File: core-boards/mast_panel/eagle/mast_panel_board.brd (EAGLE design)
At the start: 63.5 x 47.9 mm, 28 parts, among them J1 2-PIN_2MM-V, J4 4-PIN_2MM-H, U1 ATMEGA328P-AUR, U3 MCP2551T-I/SN

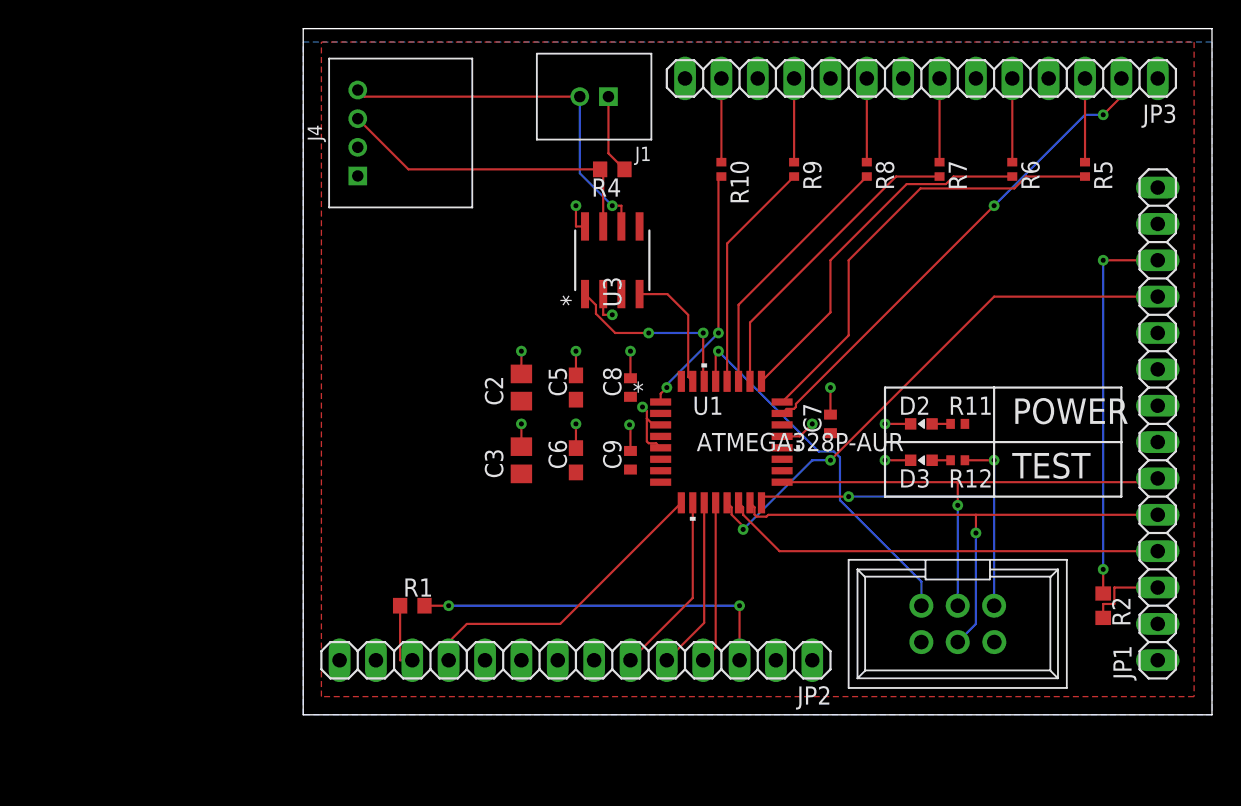
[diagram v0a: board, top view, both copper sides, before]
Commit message: 2/16/20
Cleaned up some things, added surface mount reset button
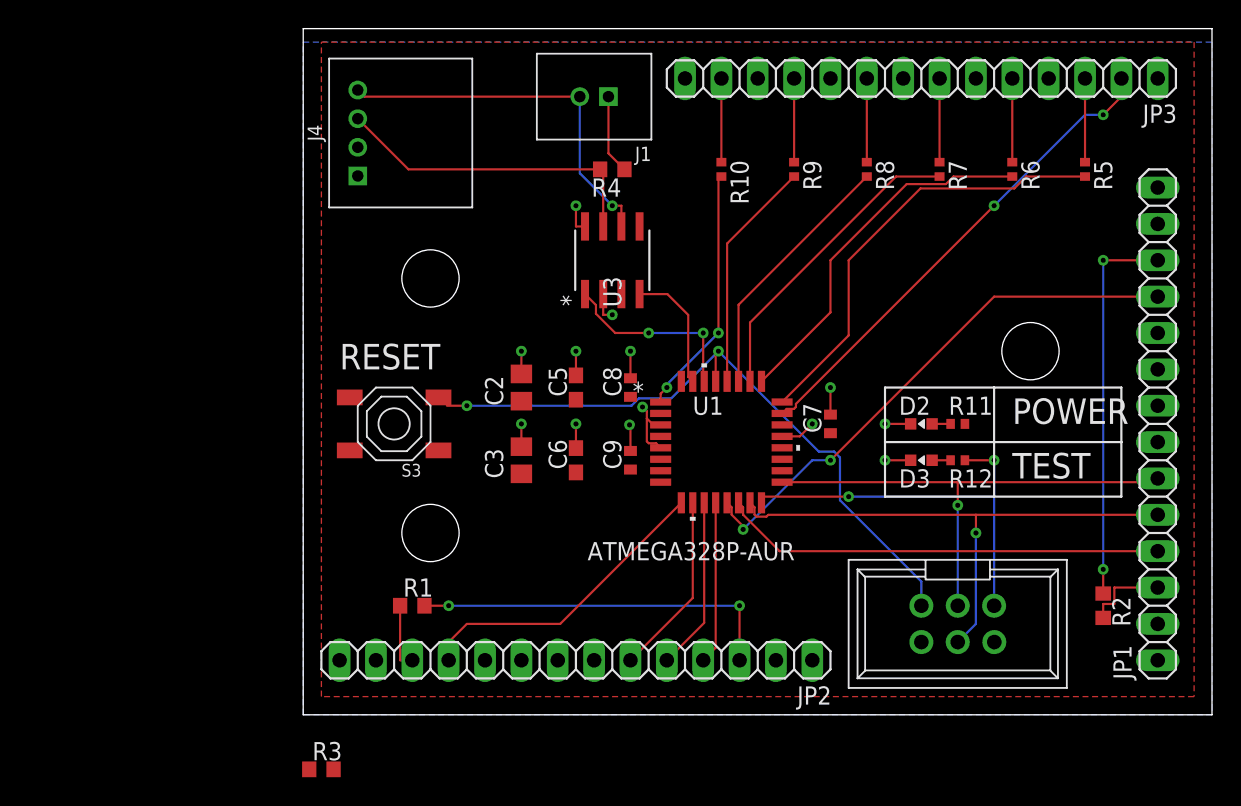
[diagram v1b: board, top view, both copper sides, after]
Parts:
- added R3: 10kO, rcl:R0603
- added S3: SKQGADE010, rgb-led:SW4-SMD-5.2X5.2X1.5MM
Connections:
- net MBED_CAN_RD/1.5C renamed MBED_CAN_RD
- net MBED_CAN_TD/1.5C renamed MBED_CAN_TD
- net +5V: now also R3.2
- net GND: now also S3.4
- net RESET: now also R3.1, S3.1
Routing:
- net RESET: track 26.6 -> 47.1 mm, vias 1 -> 2
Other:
- board text added: "RESET"
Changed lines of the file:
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@@
 <drawing>
 <settings>
-<setting alwaysvectorfont="yes"/>
+<setting alwaysvectorfont="no"/>
 <setting verticaltext="up"/>
 </settings>
-<grid distance="50" unitdist="mil" unit="mil" style="lines" multiple="1" display="no" altdistance="5" altunitdist="mil" altunit="mil"/>
+<grid distance="50" unitdist="mil" unit="mm" style="lines" multiple="1" display="no" altdistance="5" altunitdist="mil" altunit="mil"/>
 <layers>
 <layer number="1" name="Top" color="4" fill="1" visible="yes" active="yes"/>
@@
 <text x="72.39" y="25.4" size="1.778" layer="21" font="vector">POWER</text>
 <text x="72.39" y="21.59" size="1.778" layer="21" font="vector">TEST</text>
+<text x="25.4" y="29.21" size="1.778" layer="21" font="vector">RESET</text>
+<hole x="31.75" y="35.56" drill="4"/>
+<hole x="31.75" y="17.78" drill="4"/>
+<hole x="73.66" y="30.48" drill="4"/>
 </plain>
 <attributes>
@@
 <attribute name="MANUFACTURER_PART_NUMBER" value="ATMEGA328P-AUR" x="91.44" y="17.78" size="1.778" layer="27" display="off"/>
 <attribute name="NAME" x="50.0634" y="26.035" size="1.27" layer="25" font="vector" ratio="6" rot="SR0"/>
-<attribute name="VALUE" x="50.3428" y="23.495" size="1.27" layer="21" font="vector" ratio="6" rot="SR0"/>
+<attribute name="VALUE" x="42.7228" y="15.875" size="1.27" layer="21" font="vector" ratio="6" rot="SR0"/>
 <attribute name="VENDOR" value="Atmel" x="91.44" y="17.78" size="1.778" layer="27" display="off"/>
 </element>
@@
 </element>
 <element name="PROG" library="lcd-buzzer" package="2X3SHROUDED" value="ICSP Connector" x="68.58" y="11.43" smashed="yes"/>
+<element name="S3" library="rgb-led" package="SW4-SMD-5.2X5.2X1.5MM" value="SKQGADE010" x="29.21" y="25.4" smashed="yes" rot="R180">
+<attribute name="MPN" value="SKQGADE010" x="39.37" y="15.24" size="1.778" layer="27" rot="R180" display="off"/>
+<attribute name="NAME" x="31.115" y="22.606" size="0.889" layer="25" ratio="11" rot="R180"/>
+<attribute name="VALUE" x="31.115" y="29.083" size="0.889" layer="27" ratio="11" rot="R180"/>
+</element>
+<element name="R3" library="rcl" library_urn="urn:adsk.eagle:library:334" package="R0603" package3d_urn="urn:adsk.eagle:package:23555/3" value="10kO" x="24.13" y="1.27" smashed="yes">
+<attribute name="NAME" x="23.495" y="1.905" size="1.27" layer="25"/>
+<attribute name="POPULARITY" value="77" x="24.13" y="1.27" size="1.778" layer="27" display="off"/>
+<attribute name="SPICEPREFIX" value="R" x="24.13" y="1.27" size="1.778" layer="27" display="off"/>
+<attribute name="VALUE" x="23.495" y="-0.635" size="1.27" layer="27"/>
+</element>
 </elements>
 <signals>
@@
 </polygon>
 <contactref element="PROG" pad="+5V"/>
+<contactref element="R3" pad="2"/>
+<wire x1="82.55" y1="39.37" x2="82.55" y2="49.53" width="0" layer="19" extent="1-1"/>
+<wire x1="69.08" y1="25.4" x2="82.55" y2="39.37" width="0" layer="19" extent="1-1"/>
+<wire x1="59.69" y1="24.75" x2="69.08" y2="25.4" width="0" layer="19" extent="1-1"/>
+<wire x1="56.3118" y1="22.13" x2="59.69" y2="24.75" width="0" layer="19" extent="1-1"/>
+<wire x1="47.8282" y1="22.93" x2="56.3118" y2="22.13" width="0" layer="19" extent="1-1"/>
+<wire x1="47.8282" y1="24.53" x2="47.8282" y2="22.93" width="0" layer="19" extent="1-1"/>
+<wire x1="45.72" y1="22.21" x2="47.8282" y2="22.93" width="0" layer="19" extent="1-1"/>
+<wire x1="45.72" y1="27.29" x2="47.8282" y2="24.53" width="0" layer="19" extent="1-1"/>
+<wire x1="41.91" y1="27.09" x2="45.72" y2="27.29" width="0" layer="19" extent="1-1"/>
+<wire x1="38.1" y1="26.99" x2="41.91" y2="27.09" width="0" layer="19" extent="1-1"/>
+<wire x1="41.91" y1="22.01" x2="45.72" y2="22.21" width="0" layer="19" extent="1-1"/>
+<wire x1="38.1" y1="21.91" x2="41.91" y2="22.01" width="0" layer="19" extent="1-1"/>
+<wire x1="45.085" y1="34.4678" x2="45.72" y2="27.29" width="0" layer="19" extent="1-1"/>
+<wire x1="55.88" y1="8.89" x2="56.3118" y2="22.13" width="0" layer="19" extent="1-1"/>
+<wire x1="71.134" y1="10.16" x2="55.88" y2="8.89" width="0" layer="19" extent="1-1"/>
+<wire x1="82.55" y1="11.43" x2="71.134" y2="10.16" width="0" layer="19" extent="1-1"/>
+<wire x1="27.94" y1="8.89" x2="38.1" y2="21.91" width="0" layer="19" extent="1-1"/>
+<wire x1="24.98" y1="1.27" x2="27.94" y2="8.89" width="0" layer="19" extent="1-1"/>
+<wire x1="26.67" y1="42.72" x2="38.1" y2="26.99" width="0" layer="19" extent="1-1"/>
 </signal>
 <signal name="GND">
@@
 <wire x1="65.29" y1="22.86" x2="63.5" y2="22.86" width="0.1524" layer="1"/>
 <via x="63.5" y="22.86" extent="1-16" drill="0.35"/>
+<contactref element="S3" pad="4"/>
+<wire x1="74.93" y1="49.53" x2="82.55" y2="41.91" width="0" layer="19" extent="1-1"/>
+<wire x1="69.85" y1="49.53" x2="74.93" y2="49.53" width="0" layer="19" extent="1-1"/>
+<wire x1="64.77" y1="49.53" x2="69.85" y2="49.53" width="0" layer="19" extent="1-1"/>
+<wire x1="59.69" y1="49.53" x2="64.77" y2="49.53" width="0" layer="19" extent="1-1"/>
+<wire x1="54.61" y1="49.53" x2="59.69" y2="49.53" width="0" layer="19" extent="1-1"/>
+<wire x1="49.53" y1="49.53" x2="54.61" y2="49.53" width="0" layer="19" extent="1-1"/>
+<wire x1="41.91" y1="40.64" x2="49.53" y2="49.53" width="0" layer="19" extent="1-1"/>
+<wire x1="43.815" y1="34.4678" x2="42.545" y2="39.1922" width="0" layer="19" extent="1-1"/>
+<wire x1="45.72" y1="30.48" x2="44.45" y2="33.02" width="0" layer="19" extent="1-1"/>
+<wire x1="46.561" y1="26.58061875" x2="45.72" y2="28.59" width="0" layer="19" extent="1-1"/>
+<wire x1="45.65308125" y1="25.33308125" x2="46.561" y2="26.58061875" width="0" layer="19" extent="1-1"/>
+<wire x1="41.91" y1="30.48" x2="44.45" y2="33.02" width="0" layer="19" extent="1-1"/>
+<wire x1="41.91" y1="25.4" x2="41.91" y2="28.79" width="0" layer="19" extent="1-1"/>
+<wire x1="38.1" y1="30.48" x2="41.91" y2="30.48" width="0" layer="19" extent="1-1"/>
+<wire x1="38.1" y1="25.4" x2="38.1" y2="28.89" width="0" layer="19" extent="1-1"/>
+<wire x1="32.31" y1="27.25" x2="38.1" y2="28.89" width="0" layer="19" extent="1-1"/>
+<wire x1="56.3118" y1="24.53" x2="47.8282" y2="25.33" width="0" layer="19" extent="1-1"/>
+<wire x1="59.69" y1="26.05" x2="58.42" y2="25.4" width="0" layer="19" extent="1-1"/>
+<wire x1="63.5" y1="25.4" x2="59.69" y2="26.05" width="0" layer="19" extent="1-1"/>
+<wire x1="65.29" y1="22.86" x2="65.29" y2="25.4" width="0" layer="19" extent="1-1"/>
+<wire x1="66.04" y1="10.16" x2="65.29" y2="22.86" width="0" layer="19" extent="1-1"/>
+<wire x1="58.42" y1="8.89" x2="66.04" y2="10.16" width="0" layer="19" extent="1-1"/>
+<wire x1="26.67" y1="44.72" x2="41.91" y2="40.64" width="0" layer="19" extent="1-1"/>
+<wire x1="82.55" y1="8.89" x2="66.04" y2="10.16" width="0" layer="19" extent="1-1"/>
+<wire x1="25.4" y1="8.89" x2="38.1" y2="23.81" width="0" layer="19" extent="1-1"/>
 </signal>
 <signal name="BUTTON">
@@
 <wire x1="30.21" y1="43.18" x2="26.67" y2="46.72" width="0.1524" layer="1"/>
 </signal>
-<signal name="MBED_CAN_RD/1.5C">
+<signal name="MBED_CAN_RD">
 <contactref element="U3" pad="1"/>
 <contactref element="U1" pad="30"/>
@@
 <wire x1="44.65394375" y1="31.75" x2="46.99" y2="31.75" width="0.1524" layer="1"/>
 </signal>
-<signal name="MBED_CAN_TD/1.5C">
+<signal name="MBED_CAN_TD">
 <contactref element="U3" pad="4"/>
 <contactref element="U1" pad="31"/>
@@
 <wire x1="59.94135" y1="23.4668" x2="60.3532" y2="23.05495" width="0.1524" layer="16"/>
 <wire x1="60.3532" y1="23.05495" x2="60.3532" y2="20.06865" width="0.1524" layer="16"/>
+<via x="34.29" y="26.67" extent="1-16" drill="0.35"/>
+<wire x1="45.79223125" y1="26.67" x2="34.29" y2="26.67" width="0.1524" layer="16"/>
+<wire x1="46.30965" y1="27.18741875" x2="45.79223125" y2="26.67" width="0.1524" layer="16"/>
+<wire x1="51.8632" y1="30.48" x2="48.57061875" y2="27.18741875" width="0.1524" layer="16"/>
+<wire x1="48.57061875" y1="27.18741875" x2="46.30965" y2="27.18741875" width="0.1524" layer="16"/>
+<wire x1="34.29" y1="26.67" x2="32.89" y2="26.67" width="0.1524" layer="1"/>
+<contactref element="S3" pad="1"/>
+<contactref element="R3" pad="1"/>
+<wire x1="32.31" y1="23.55" x2="32.89" y2="26.67" width="0" layer="19" extent="1-1"/>
+<wire x1="23.28" y1="1.27" x2="32.31" y2="23.55" width="0" layer="19" extent="1-1"/>
 </signal>
 </signals>

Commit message: 2/23/19
Changed out resistors, fixed SPI connections on board
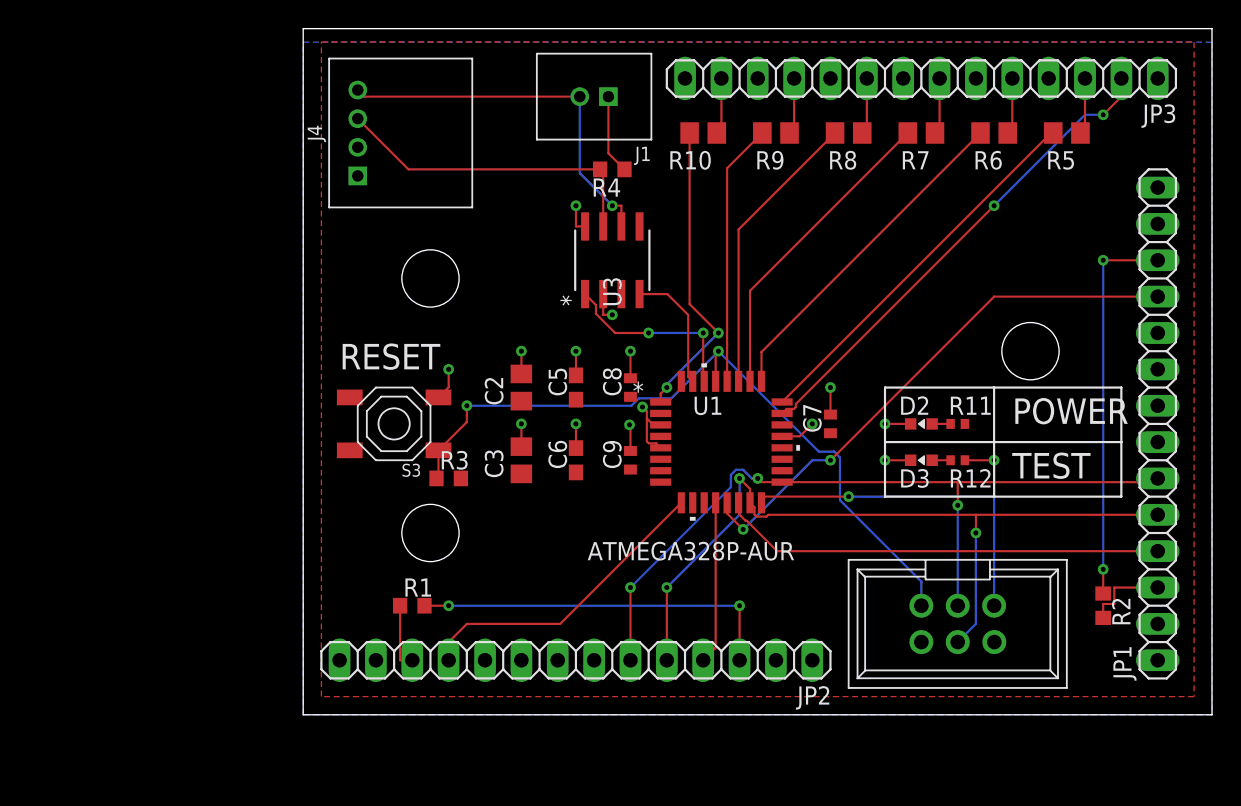
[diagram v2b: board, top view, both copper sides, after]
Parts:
- R10, R5, R6, R7, R8, R9: value 100 -> 50kO; device rcl:R0402 -> rcl:R0805
- moved R3 22.2 mm to (33.0, 21.6)
- moved R10 2.84 mm to (50.8, 45.7), turned to 180 degrees
- moved R5 2.84 mm to (76.2, 45.7), turned to 180 degrees
- moved R6 2.84 mm to (71.1, 45.7), turned to 180 degrees
- moved R7 2.84 mm to (66.0, 45.7), turned to 180 degrees
- moved R8 2.84 mm to (61.0, 45.7), turned to 180 degrees
- moved R9 2.84 mm to (55.9, 45.7), turned to 180 degrees
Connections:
- removed net LCD1_MOSI: JP1.5, PROG.MOSI, U1.15
- removed net LCD1_SCLK: JP1.6, PROG.SCK, U1.17
- removed net LCD2_MOSI: JP2.5, U1.11
- removed net LCD2_SCLK: JP2.6, U1.10
- new net LCD_MOSI: JP1.5, JP2.5, PROG.MOSI, U1.15
- new net LCD_SCLK: JP1.6, JP2.6, PROG.SCK, U1.17
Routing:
- net LCD_MOSI: track 0.00 -> 55.5 mm, vias 0 -> 3
- net LCD_SCLK: track 0.00 -> 54.9 mm, vias 0 -> 3
- net LCD1_MOSI: track 38.6 -> 0.00 mm, vias 1 -> 0
- net LCD1_SCLK: track 35.0 -> 0.00 mm, vias 1 -> 0
- net LCD2_SCLK: track 12.8 -> 0.00 mm
- net LCD2_MOSI: track 12.1 -> 0.00 mm
- net RESET: track 47.1 -> 51.7 mm
- net LED_CTRL1: track 30.8 -> 26.7 mm
- net LED_CTRL6: track 17.5 -> 21.3 mm
- net GND: track 27.2 -> 29.5 mm, vias 13 -> 14
- net LED_CTRL5: track 16.2 -> 18.4 mm
- net LED_CTRL4: track 18.0 -> 20.1 mm
- net LED1: track 5.85 -> 3.94 mm
- net LED6: track 5.85 -> 3.94 mm
- net LED5: track 5.85 -> 3.94 mm
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
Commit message: 3/1/2020
Switched out CAN connector, cleaned up a few things
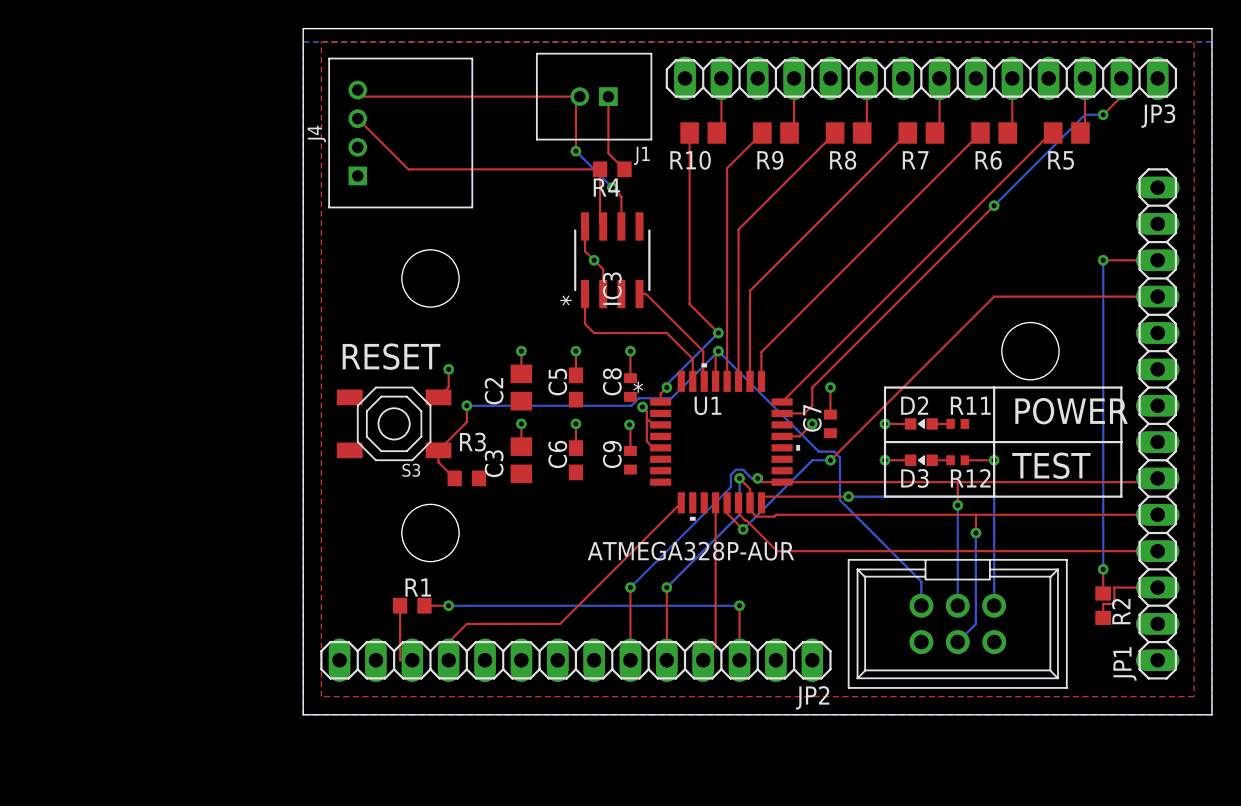
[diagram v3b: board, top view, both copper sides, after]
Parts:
- moved R3 1.27 mm to (34.3, 21.6)
- renumbered U3 to IC3
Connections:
- net MBED_CAN_RD: now also IC3.4; no longer IC3.1
- net MBED_CAN_TD: now also IC3.1; no longer IC3.4
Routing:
- net MBED_CAN_RD: track 13.1 -> 8.23 mm, vias 2 -> 0
- net MBED_CAN_TD: track 8.77 -> 12.2 mm
- net GND: track 29.5 -> 30.6 mm, vias 14 -> 13
- net BUTTON: track 34.3 -> 34.9 mm
- net CAN_N: track 26.3 -> 26.9 mm, vias 1 -> 2

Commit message: Revert "3/1/2020"
This reverts commit 3611e6968998cfd50a97478803bccb5be4cedb33.
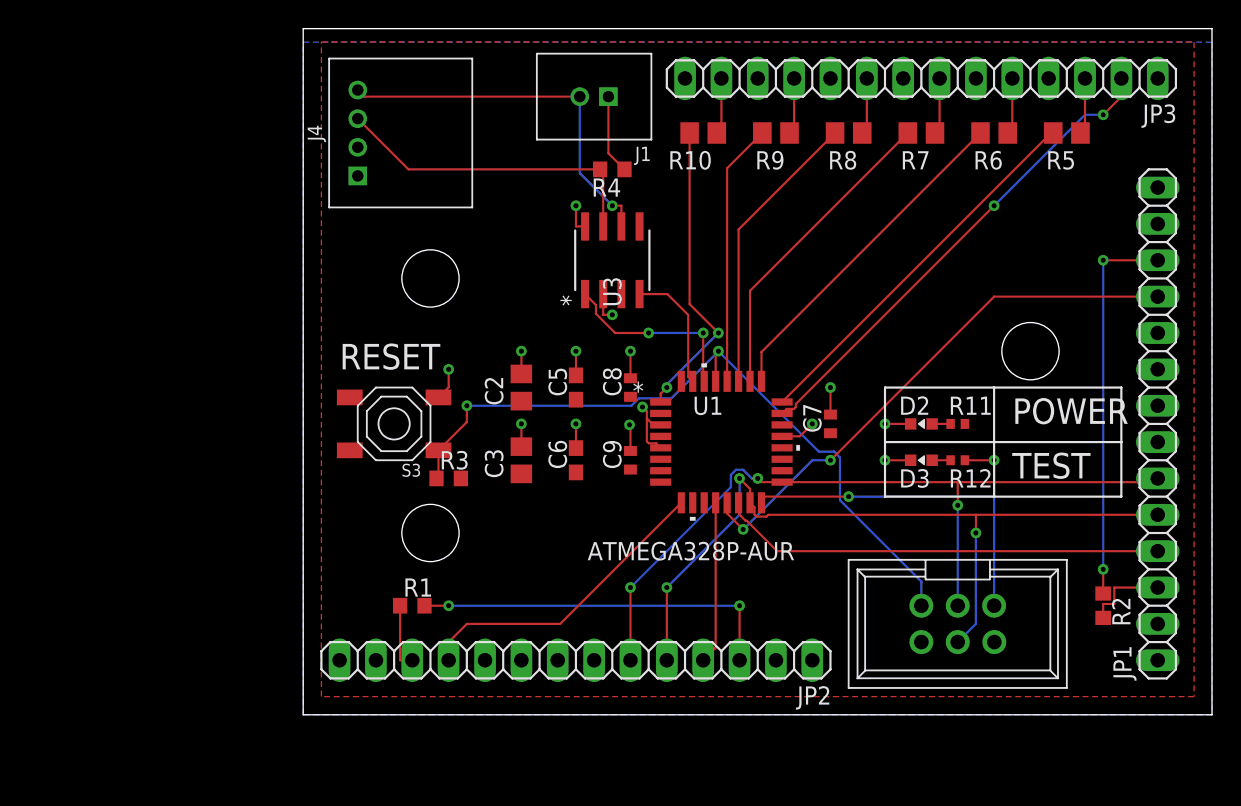
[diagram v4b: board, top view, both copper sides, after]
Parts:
- moved R3 1.27 mm to (33.0, 21.6)
- renumbered IC3 to U3
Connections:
- net MBED_CAN_RD: now also U3.1; no longer U3.4
- net MBED_CAN_TD: now also U3.4; no longer U3.1
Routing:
- net MBED_CAN_RD: track 8.23 -> 13.1 mm, vias 0 -> 2
- net MBED_CAN_TD: track 12.2 -> 8.77 mm
- net GND: track 30.6 -> 29.5 mm, vias 13 -> 14
- net BUTTON: track 34.9 -> 34.3 mm
- net CAN_N: track 26.9 -> 26.3 mm, vias 2 -> 1
